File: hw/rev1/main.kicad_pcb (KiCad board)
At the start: 2 copper layers, 80 x 130 mm, 118 parts, among them J1 80VAC, J10 NSM E-004 Counter power/speed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, J11 NSM E-004 Counter power & RS4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, J2 CAP, J3 MOTOR, J4 POWER, J5 TACHO, J6 AVR-ISP-6, J7 NSM E-004 Controller RS485, J8 Conn_01x05, J9 Speed/reverse, Q1 IRF740, Q2 2N5551, Q3 К504НТ3А, Q4 2N5551, U1 LM324, U2 LM311, U3 ATmega168-20AU, U4 ADM485AR, Y1 20MHz

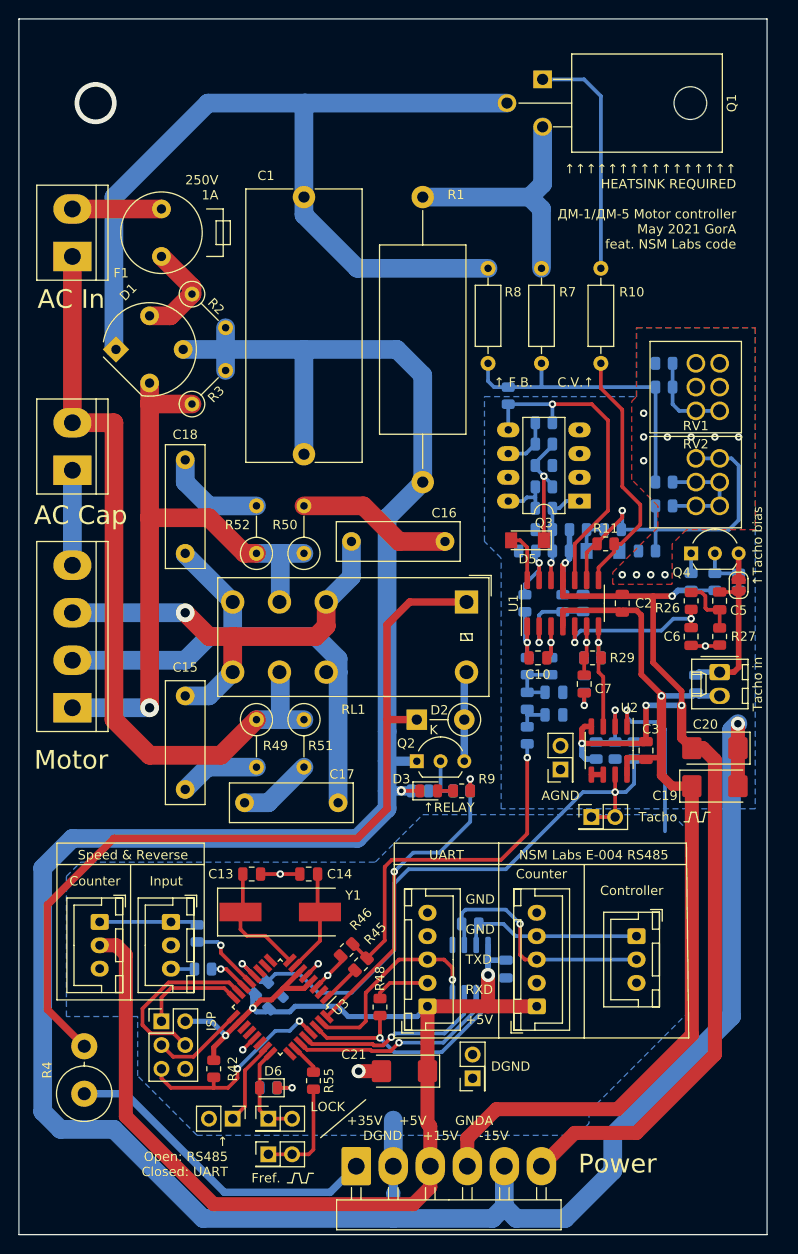
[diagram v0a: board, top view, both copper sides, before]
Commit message: Добавлена печатная плата rev1 (вероятно чистовая).
+ Обозначена и разведена схема ZCD;
+ Исключена схема аналогового перемножителя;
  * модуляция модулем синуса полностью цифровая;
+ LM324 использована полностью:
  * собран 2й PWM фильтр, подключенный к OC2A в отладочных целях;
+ Добавлен доп. светодиод, предназначенный для контроля за ZCD;
+ Исправлен разъем логических сигналов управления;
+ Всякие незначимые украшательства.
+ Немного документирована плата rev0.
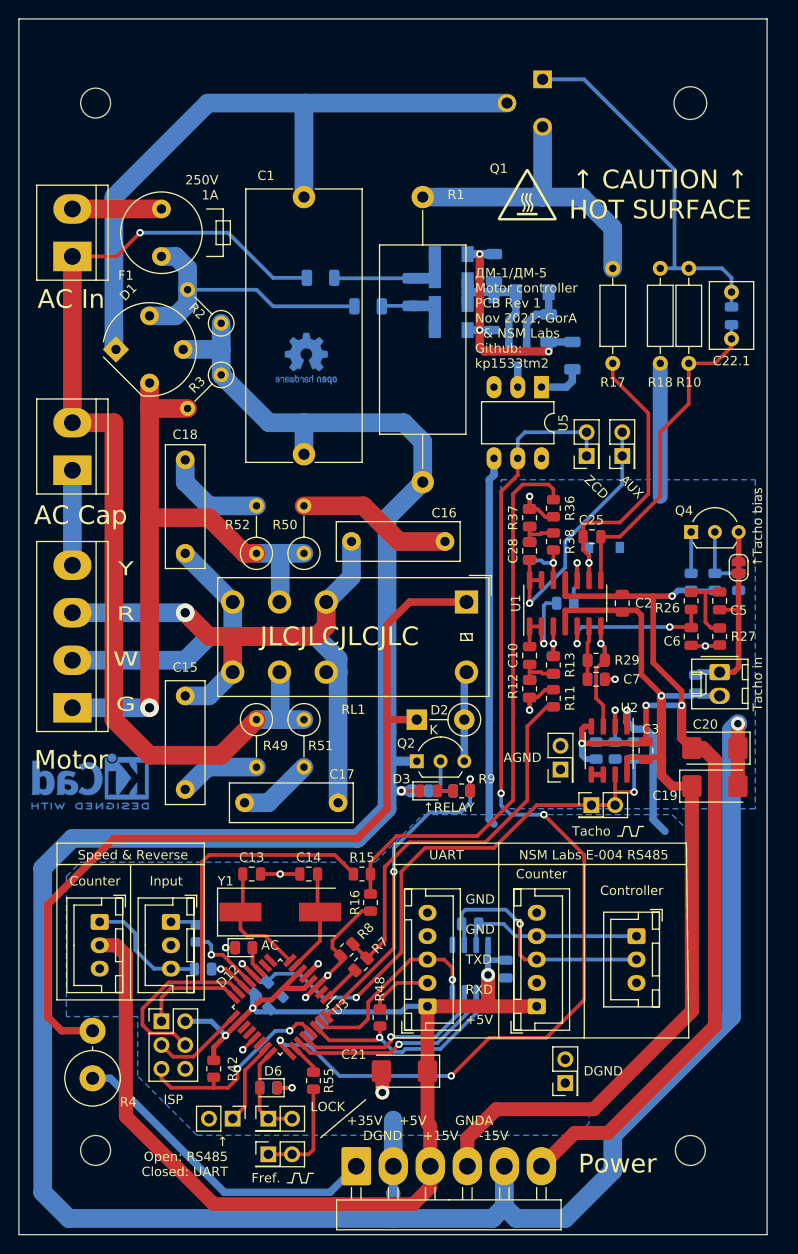
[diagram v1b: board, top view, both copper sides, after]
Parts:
- removed R40: 3k*, Resistor_SMD:R_0805_2012Metric
- removed R41: DNP, Resistor_SMD:R_0805_2012Metric
- removed R44: 110k*, Resistor_SMD:R_0805_2012Metric
- removed R45: 11k*, Resistor_SMD:R_0805_2012Metric
- removed R46: 1k5*, Resistor_SMD:R_0805_2012Metric
- removed RF1, RF2, RF3, RF4: *, Resistor_SMD:R_0805_2012Metric
- removed RV1: 220k, pot_universal:Potentiometer_Bourns_Universal
- removed RV2: 2k2, pot_universal:Potentiometer_Bourns_Universal
- added C22.1: 680p, Capacitor_THT:C_Rect_L7.0mm_W4.5mm_P5.00mm, F.Cu at (106.2, 59.2)
- added C22.2: 680p, Capacitor_SMD:C_0805_2012Metric, B.Cu at (106.2, 61.8)
- added C23: 1n, Capacitor_SMD:C_1206_3216Metric, B.Cu at (71.9, 59.2)
- added C24: 10u, Capacitor_SMD:C_1206_3216Metric, B.Cu at (86.6, 63.1)
- added C25: DNP, Capacitor_SMD:C_0805_2012Metric, F.Cu at (91.3, 85.4)
- added C26: 15n, Capacitor_SMD:C_0805_2012Metric, B.Cu at (84.6, 83.3)
- added C27: 100p, Capacitor_SMD:C_0805_2012Metric, B.Cu at (84.6, 86.9)
- added C28: 15n, Capacitor_SMD:C_0805_2012Metric, F.Cu at (84.6, 86.9)
- added D10: LL4148, Diode_SMD:D_MiniMELF, B.Cu at (84.9, 59.2)
- added D11: 15V, Diode_SMD:D_SOD-123, B.Cu at (80.8, 61.6)
- added D12: LOCK, LED_SMD:LED_0805_2012Metric, F.Cu at (54.1, 129.3)
- added D7: LL4148, Diode_SMD:D_MiniMELF, B.Cu at (76.2, 60.5)
- added D8: LL4148, Diode_SMD:D_MiniMELF, B.Cu at (76.2, 55.1)
- added D9: LL4148, Diode_SMD:D_MiniMELF, B.Cu at (76.2, 57.9)
- added G***: LOGO, img:hot, F.Cu at (84.4, 48.8)
- added H1: MountingHole, MountingHole:MountingHole_3.2mm_M3, F.Cu at (38.2, 151.0)
- added H2: MountingHole, MountingHole:MountingHole_3.2mm_M3, F.Cu at (101.8, 151.0)
- added H3: MountingHole, MountingHole:MountingHole_3.2mm_M3, F.Cu at (38.2, 39.0)
- added REF**: OSHW-Logo2_7.3x6mm_Copper, Symbol:OSHW-Logo2_7.3x6mm_Copper, B.Cu at (60.7, 66.3)
- added REF**: KiCad-Logo2_5mm_Copper, Symbol:KiCad-Logo2_5mm_Copper, B.Cu at (37.6, 111.5)
- added TP6: TEST POINT AUX, Connector_PinHeader_2.54mm:PinHeader_2x01_P2.54mm_Vertical, F.Cu at (94.5, 76.7)
- added TP7: TEST POINT ZCD, Connector_PinHeader_2.54mm:PinHeader_2x01_P2.54mm_Vertical, F.Cu at (90.7, 76.7)
- added U5: CNY17-2, Package_DIP:DIP-6_W7.62mm_LongPads, F.Cu at (85.9, 69.4)
- C10: value 27n -> 15n
- C8: value 220n -> 15n
- C9: value 220n -> 100p
- D4: value LL4148 -> DNP; footprint Diode_SMD:D_MiniMELF -> Diode_SMD:D_SOD-123
- D5: moved to B.Cu
- J8: value Conn_01x05 -> UART
- Q1: value IRF740 -> 6N60C; footprint to220:TO-220F-3_Horizontal_TabDown -> to220:TO-220F-3_Horizontal_TabDown_no_silk
- Q3: value К504НТ3А -> BC847; footprint Package_DIP:DIP-8_W7.62mm_LongPads -> Package_TO_SOT_SMD:SOT-23; moved to B.Cu
- R10: value 2k7 -> 3k
- R11: value 150k -> 8k2
- R12: value 150k -> 27k; moved to F.Cu
- R13: value 1k8 -> 27k; moved to F.Cu
- R14: value 2k7 -> 0
- R15: moved to F.Cu
- R16: value 120k -> 36k; moved to F.Cu
- R17: value 1M -> 10k; footprint Resistor_SMD:R_0805_2012Metric -> Resistor_THT:R_Axial_DIN0207_L6.3mm_D2.5mm_P10.16mm_Horizontal; moved to F.Cu
- R18: value 1M -> 9k1; footprint Resistor_SMD:R_0805_2012Metric -> Resistor_THT:R_Axial_DIN0207_L6.3mm_D2.5mm_P10.16mm_Horizontal; moved to F.Cu
- R19, R20: value 1M -> 33k; footprint Resistor_SMD:R_0805_2012Metric -> Resistor_SMD:R_1206_3216Metric
- R21: value 10k -> 22k; footprint Resistor_SMD:R_0805_2012Metric -> Resistor_SMD:R_1206_3216Metric
- R22: value 10k -> 1k; footprint Resistor_SMD:R_0805_2012Metric -> Resistor_SMD:R_1206_3216Metric
- R35: value 36k -> 20k
- R36: value 36k -> 8k2; moved to F.Cu
- R37, R38: value 36k -> 27k; moved to F.Cu
- R39: value 100k -> 330*
- R43, R9: value 330 -> 330*
- R7: value 8k2 -> 10k; footprint Resistor_THT:R_Axial_DIN0207_L6.3mm_D2.5mm_P10.16mm_Horizontal -> Resistor_SMD:R_0805_2012Metric
- R8: value 150k -> 36k; footprint Resistor_THT:R_Axial_DIN0207_L6.3mm_D2.5mm_P10.16mm_Horizontal -> Resistor_SMD:R_0805_2012Metric
- Y1: value 20MHz -> 16MHz
- moved R8 74.4 mm to (65.1, 129.6), turned to 45 degrees
- moved R7 67.1 mm to (66.6, 131.1), turned to 225 degrees
- moved R39 47.5 mm to (54.1, 129.3), turned to 0 degrees
- moved R16 42.8 mm to (67.6, 124.5), turned to 90 degrees
- moved R15 41.7 mm to (66.7, 121.4)
- moved R35 38.6 mm to (61.8, 137.9), turned to 45 degrees
- moved R20 34.3 mm to (62.3, 57.7), turned to 0 degrees
- moved R19 26.9 mm to (67.3, 60.7)
- moved D5 23.9 mm to (76.2, 63.3)
- moved R18 22.5 mm to (98.6, 56.7), turned to 270 degrees
- moved R21 21.8 mm to (80.8, 56.6), turned to 270 degrees
- moved R36 20.8 mm to (87.2, 82.3), turned to 90 degrees
- moved R12 19.2 mm to (84.6, 101.6), turned to 270 degrees
- moved R17 18.1 mm to (93.5, 56.7), turned to 270 degrees
- moved R11 17.4 mm to (87.2, 102.6), turned to 270 degrees
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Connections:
- net /Motor Output/+35V renamed +36V
- net /Motor Output/485\~UART renamed /485\~UART
- net /Motor Output/A renamed /A
- net /Motor Output/B renamed /B
- net /Motor Output/DE renamed /DE
- net /Motor Output/DIR renamed /DIR
- net /Motor Output/LOCK renamed /LOCK
- net /Motor Output/M_RED renamed /analog section/M_RED
- net /Motor Output/M_WHITE renamed /analog section/M_WHITE
- net /Motor Output/M_YELLOW renamed /analog section/M_YELLOW
- net /Motor Output/REF renamed /REF
- net /Motor Output/REVERSE renamed /REVERSE
- net /Motor Output/RXD renamed /RXD
- net /Motor Output/SPEED renamed /SPEED
- net /Motor Output/TACHO renamed /TACHO
- net /Motor Output/TXD renamed /TXD
- net /Motor Output/~RE renamed /~RE
- C1 pad 1: /Motor Output/DC1 -> Net-(C1-Pad1)
- C5 pad 1: Net-(C5-Pad1) -> Net-(C4-Pad2)
- C5 pad 2: Net-(C4-Pad2) -> Net-(C5-Pad2)
- D1 pad 1: /Motor Output/DC1 -> Net-(C1-Pad1)
- D1 pad 2: /Motor Output/AC2 -> /analog section/M_GREEN
- D4 pad 1: Net-(D4-Pad1) -> Net-(C25-Pad2)
- D5 pad 1: Net-(D5-Pad1) -> Net-(C24-Pad1)
- D5 pad 2: Net-(D5-Pad2) -> Net-(C23-Pad1)
- F1 pad 1: Net-(D1-Pad4) -> Net-(F1-Pad1)
- F1 pad 2: /Motor Output/AC3 -> Net-(D1-Pad4)
- J1 pad 1: /Motor Output/AC1 -> Net-(J1-Pad1)
- J1 pad 2: /Motor Output/AC3 -> Net-(F1-Pad1)
- J2 pad 2: /Motor Output/AC1 -> Net-(J1-Pad1)
- J3 pad 1: /Motor Output/AC2 -> /analog section/M_GREEN
- J6 pad 4: Net-(J6-Pad4) -> /MOSI\DEBUG_PWM
- J9 pad 1: Net-(J10-Pad1) -> Net-(J9-Pad1)
- J9 pad 3: Net-(J9-Pad3) -> Net-(J10-Pad1)
- Q1 pad 1: Net-(Q1-Pad1) -> Net-(C22.1-Pad1)
- Q1 pad 2: /Motor Output/DC1 -> Net-(C1-Pad1)
- Q3 pad 1: Net-(Q3-Pad1) -> Net-(D10-Pad1)
- Q3 pad 2: GNDA -> Net-(C24-Pad2)
- Q3 pad 3: GNDA -> Net-(Q3-Pad3)
- R10 pad 1: Net-(Q1-Pad1) -> Net-(C22.1-Pad1)
- R10 pad 2: Net-(R10-Pad2) -> Net-(C22.1-Pad2)
- R11 pad 1: Net-(R11-Pad1) -> Net-(C8-Pad1)
- R11 pad 2: Net-(R10-Pad2) -> Net-(R11-Pad2)
- R12 pad 1: Net-(D4-Pad1) -> Net-(C10-Pad2)
- R12 pad 2: Net-(R11-Pad1) -> Net-(C8-Pad1)
- R13 pad 1: GNDA -> Net-(C9-Pad1)
- R13 pad 2: Net-(R11-Pad1) -> Net-(C10-Pad2)
- R14 pad 1: -15V -> Net-(C10-Pad1)
- R14 pad 2: Net-(D4-Pad1) -> Net-(R14-Pad2)
- R15 pad 1: Net-(Q3-Pad1) -> Net-(R15-Pad1)
- R15 pad 2: GNDA -> /MOSI\DEBUG_PWM
- R16 pad 1: -15V -> GNDD
- R16 pad 2: Net-(Q3-Pad1) -> Net-(R15-Pad1)
- R17 pad 1: Net-(Q3-Pad6) -> Net-(Q1-Pad3)
- R17 pad 2: Net-(Q3-Pad5) -> Net-(C25-Pad2)
- R18 pad 1: Net-(D5-Pad1) -> Net-(C22.1-Pad1)
- R18 pad 2: Net-(Q3-Pad6) -> GNDA
- R19 pad 1: Net-(Q3-Pad8) -> Net-(D1-Pad4)
- R19 pad 2: Net-(D5-Pad1) -> Net-(C23-Pad1)
- R2 pad 1: Net-(D1-Pad4) -> GNDA
- R2 pad 2: GNDA -> Net-(D1-Pad4)
- R20 pad 1: Net-(Q3-Pad1) -> Net-(J1-Pad1)
- R20 pad 2: Net-(Q3-Pad8) -> Net-(C23-Pad2)
- R21 pad 1: GNDA -> Net-(C24-Pad1)
- R21 pad 2: Net-(D5-Pad1) -> Net-(D10-Pad1)
- R22 pad 1: Net-(Q3-Pad5) -> Net-(R22-Pad1)
- R22 pad 2: Net-(R22-Pad2) -> Net-(C24-Pad1)
- R26 pad 1: Net-(C5-Pad1) -> Net-(C6-Pad1)
- R26 pad 2: Net-(C6-Pad1) -> Net-(C5-Pad2)
- R27 pad 2: Net-(C5-Pad1) -> Net-(C5-Pad2)
- R3 pad 1: /Motor Output/AC2 -> GNDA
- R3 pad 2: GNDA -> /analog section/M_GREEN
- R35 pad 1: Net-(C8-Pad1) -> /ZCD
- R35 pad 2: Net-(R35-Pad2) -> +5V
- R36 pad 1: Net-(C9-Pad1) -> Net-(C26-Pad1)
- R36 pad 2: Net-(C8-Pad1) -> Net-(R15-Pad1)
- R37 pad 1: Net-(C10-Pad1) -> Net-(C28-Pad2)
- R37 pad 2: Net-(C9-Pad1) -> Net-(C26-Pad1)
- R38 pad 1: Net-(C10-Pad2) -> Net-(C27-Pad1)
- R38 pad 2: Net-(C9-Pad1) -> Net-(C28-Pad2)
- R39 pad 1: Net-(C10-Pad1) -> Net-(D12-Pad1)
- R39 pad 2: Net-(R39-Pad2) -> GNDD
- R49 pad 1: /Motor Output/AC1 -> Net-(J1-Pad1)
- R50 pad 1: /Motor Output/AC2 -> /analog section/M_GREEN
- R51 pad 1: /Motor Output/AC1 -> Net-(J1-Pad1)
- R52 pad 1: /Motor Output/AC2 -> /analog section/M_GREEN
- R53 pad 1: Net-(J10-Pad1) -> Net-(J9-Pad1)
- R54 pad 1: Net-(J9-Pad3) -> Net-(J10-Pad1)
- R7 pad 1: Net-(R22-Pad2) -> Net-(R11-Pad2)
- R7 pad 2: Net-(Q1-Pad3) -> /PWM
- R8 pad 1: /Motor Output/DC1 -> GNDD
- R8 pad 2: Net-(R22-Pad2) -> Net-(R11-Pad2)
- RL1 pad 3: /Motor Output/AC2 -> /analog section/M_GREEN
- RL1 pad 6: /Motor Output/AC1 -> Net-(J1-Pad1)
- U1 pad 10: Net-(Q3-Pad5) -> Net-(R14-Pad2)
- U1 pad 12: Net-(Q3-Pad1) -> Net-(C27-Pad1)
- U1 pad 13: Net-(R39-Pad2) -> /AUX
- U1 pad 14: Net-(D5-Pad2) -> /AUX
- U1 pad 2: Net-(R40-Pad1) -> Net-(C10-Pad1)
- U1 pad 3: Net-(C10-Pad2) -> Net-(C9-Pad1)
- U1 pad 8: Net-(R10-Pad2) -> Net-(C22.1-Pad2)
- U1 pad 9: Net-(R11-Pad1) -> Net-(C25-Pad2)
- U3 pad 1: /Motor Output/PWM -> /PWM
- U3 pad 11: Net-(U3-Pad11) -> /AC_GOOD
- U3 pad 15: Net-(J6-Pad4) -> /MOSI\DEBUG_PWM
- U3 pad 25: Net-(U3-Pad25) -> /ZCD
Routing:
- net /ZCD: track 0.00 -> 117.2 mm, vias 0 -> 4
- net Net-(J1-Pad1): track 0.00 -> 110.7 mm, vias 0 -> 1
- net /Motor Output/DC1: track 96.6 -> 0.00 mm
- net /Motor Output/AC1: track 82.6 -> 0.00 mm
- net Net-(C1-Pad1): track 0.00 -> 72.7 mm
- net /Motor Output/AC2: track 70.9 -> 0.00 mm, vias 1 -> 0
- net /analog section/M_GREEN: track 0.00 -> 70.4 mm, vias 0 -> 1
- net Net-(R15-Pad1): track 0.00 -> 60.2 mm
- net /MOSI\DEBUG_PWM: track 0.00 -> 49.4 mm
- net GNDD: track 40.5 -> 88.0 mm, vias 6 -> 7
- net Net-(R11-Pad2): track 0.00 -> 42.5 mm
- net Net-(C22.1-Pad1): track 0.00 -> 39.8 mm
- net Net-(R11-Pad1): track 39.7 -> 0.00 mm, vias 1 -> 0
- net Net-(R35-Pad2): track 39.0 -> 0.00 mm, vias 1 -> 0
- net Net-(C22.1-Pad2): track 0.00 -> 35.9 mm
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- removed copper zone on F.Cu, net GNDA
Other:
- board text added: "AC"
- board text added: "AUX"
- board text added: "JLCJLCJLCJLC"
- board text added: "TODO: + Q1 Staggered pins (or cut between) + 2 M3 holes on the corner + optional grounds join + RS485/UART switch ? GND vias, a LOT of them (gnd single layer only) + spark suppression + fuse? ? AC input protection? bidir TVS? Zener?"
- board text added: "Y R W G"
- board text added: "ZCD"
- board text added: "ДМ-1/ДМ-5 Motor controller PCB Rev 1 Nov 2021; GorA & NSM Labs Github: kp1533tm2"
- board text added: "↑ CAUTION ↑ HOT SURFACE"
- board text removed: "TODO: + Q1 Staggered pins (or cut between) + 2 M3 holes on the corner + optional grounds join + RS485/UART switch ? GND vias, a LOT of them (gnd single layer only) + spark suppression + fuse?"
- board text removed: "↑ F.B. C.V.↑"
- board text removed: "↑↑↑↑↑↑↑↑↑↑↑↑↑↑↑↑ HEATSINK REQUIRED ДМ-1/ДМ-5 Motor controller May 2021 GorA feat. NSM Labs code"
